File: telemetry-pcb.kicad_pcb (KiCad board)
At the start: 2 copper layers, 120 x 70 mm, 62 parts, among them CN1 12V, CN2 CAN, CN3 RS232, CN4 UART, CN5 THERMO1, CN6 THERMO2, CN7 CAN, IC1 MAX3232CPWR, IC2 MAX31855K, IC3 MAX31855K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

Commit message: added bottom silkscreen logo, date, and names
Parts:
- added G***: LOGO, telemetry-pcb:supermileage_logo, B.Cu at (104.9, 101.2)
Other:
- board text added: "Mar 4, 2022"
- board text added: "Silviu Toderita Leslie Cheng Valentino Jaber Colby Sparks Apoorv Garg"
- board text added: "Telemetry 2.0"

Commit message: deleted extraneous footprints
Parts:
- removed G***: LOGO, telemetry-pcb:supermileage_logo

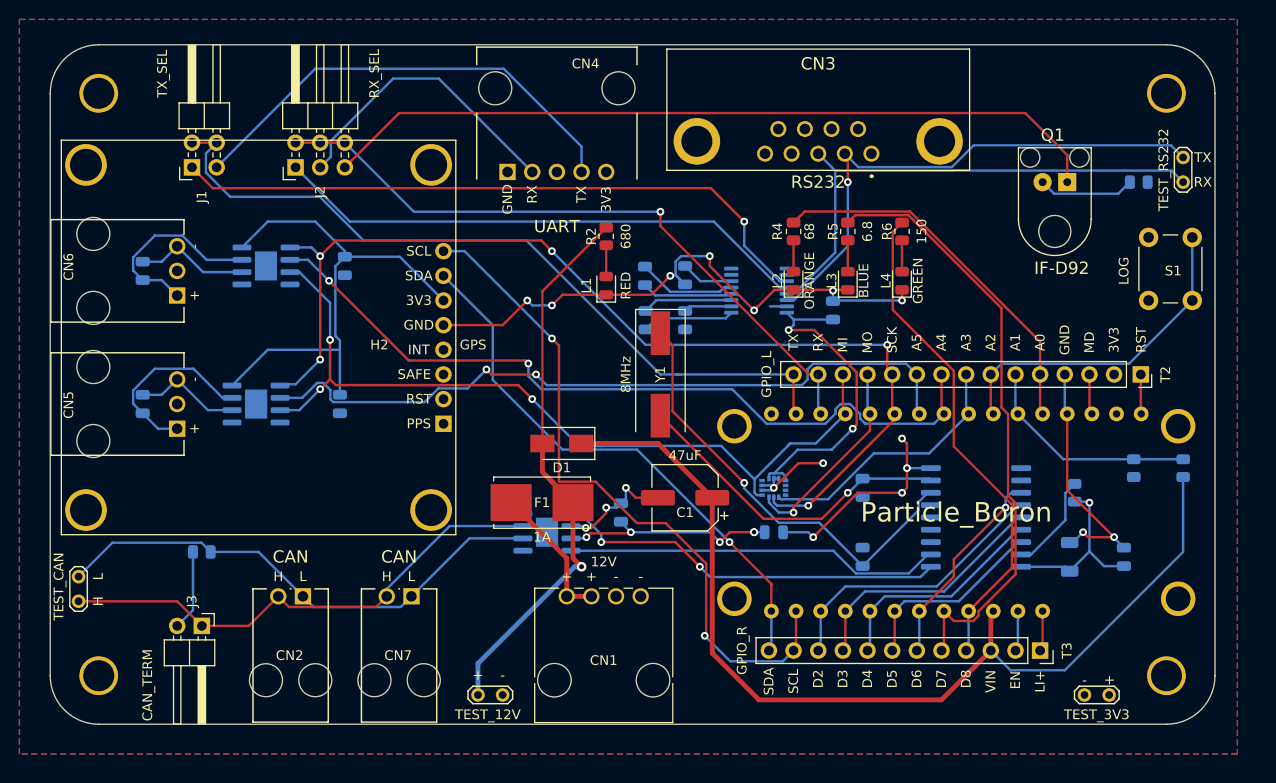
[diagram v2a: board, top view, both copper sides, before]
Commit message: Shrinks board and removes GPS. Replaces GPS with Qwiic connector for off-board GPS
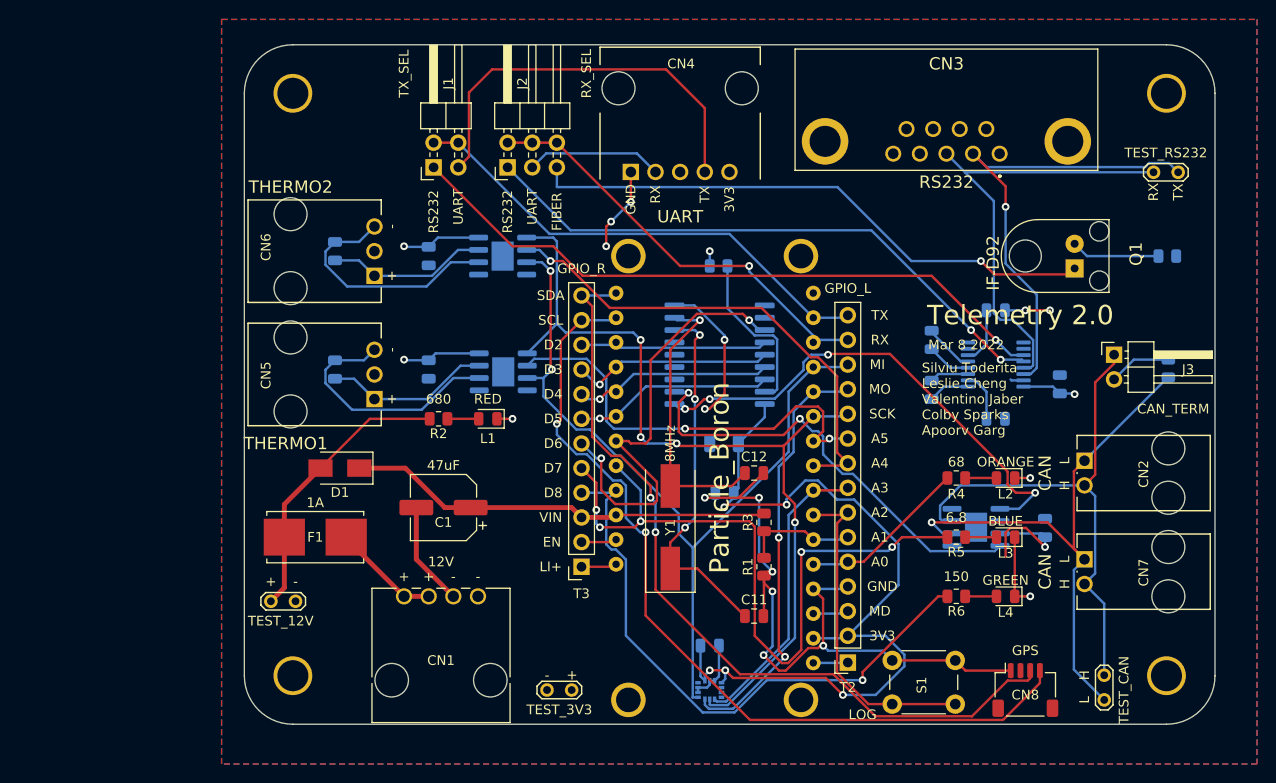
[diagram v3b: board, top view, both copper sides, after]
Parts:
- removed H2: GPS, telemetry-pcb:Sparkfun GPS
- added CN8: GPS, Connector_JST:JST_SH_SM04B-SRSS-TB_1x04-1MP_P1.00mm_Horizontal, F.Cu at (170.5, 121.5)
- added G***: LOGO, Footprints:sm-logo-small, B.Cu at (107.0, 102.7)
- C11, C12, R1, R3: moved to F.Cu
- moved T6 106.4 mm to (178.6, 122.5), turned to 90 degrees
- moved R9 101.3 mm to (185.2, 88.4), turned to 270 degrees
- moved J3 98.0 mm to (179.6, 86.9), turned to 0 degrees
- moved CN2 89.9 mm to (182.7, 99.1), turned to 90 degrees
- moved CN7 77.2 mm to (182.7, 109.3), turned to 90 degrees
- moved T4 55.4 mm to (123.7, 121.5)
- moved T3 48.0 mm to (124.7, 108.8), turned to 180 degrees
- moved S1 45.5 mm to (156.7, 118.4), turned to 0 degrees
- moved IC5 44.2 mm to (165.4, 104.7)
- moved C16 43.7 mm to (172.5, 104.8)
- moved R3 43.5 mm to (143.5, 104.2), turned to 90 degrees
- moved R8 43.5 mm to (138.9, 77.8), turned to 180 degrees
- moved T2 42.0 mm to (152.2, 118.4), turned to 180 degrees
- moved C13 41.7 mm to (139.5, 101.2), turned to 0 degrees
- moved R1 39.4 mm to (143.5, 108.8)
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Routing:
- net /VIN: track 102.2 -> 44.0 mm
- net /A4: track 81.9 -> 50.4 mm, vias 2 -> 1
- net /A5: track 75.8 -> 44.6 mm
- net /TX: track 80.0 -> 50.2 mm
- net Net-(D1-Pad2): track 57.6 -> 29.2 mm, vias 1 -> 0
- net /SDA: track 57.2 -> 84.1 mm, vias 1 -> 2
- net /D6: track 21.3 -> 46.7 mm, vias 1 -> 2
- net /RX: track 68.8 -> 44.4 mm
- net /MO: track 21.1 -> 43.9 mm, vias 1 -> 2
- net Net-(J2-Pad5): track 81.3 -> 59.4 mm, vias 0 -> 1
- net /A0: track 39.0 -> 17.5 mm
- net /SCL: track 71.0 -> 88.3 mm
- net /SCK: track 107.7 -> 91.0 mm, vias 5 -> 4
- net Net-(CN4-Pad2): track 30.6 -> 14.1 mm
- net Net-(C7-Pad1): track 11.2 -> 25.6 mm
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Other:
- board size 120 x 70 mm -> 100 x 70 mm
- board text added: "Mar 8 2022"
- board text removed: "Mar 4, 2022"

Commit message: changes CAN ports to 3 pin, Thermocouple ports to 2 pin
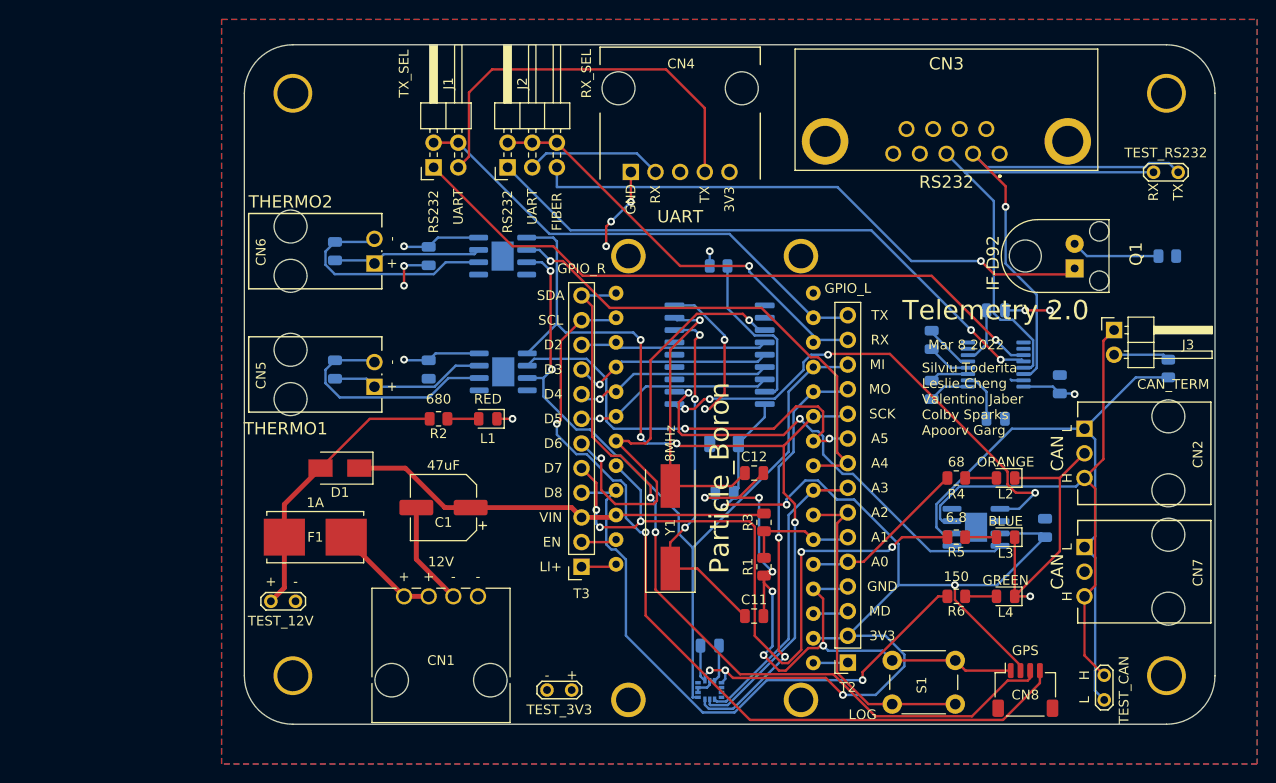
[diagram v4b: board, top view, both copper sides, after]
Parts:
- CN2, CN7: footprint telemetry-pcb:molex_sl_1x02_horizontal -> telemetry-pcb:molex-sl-1x03-horizontal
- CN5, CN6: footprint telemetry-pcb:molex-sl-1x03-horizontal -> telemetry-pcb:molex_sl_1x02_horizontal
- moved J3 2.54 mm to (179.6, 84.4)
- moved CN2 2.03 mm to (182.7, 97.1)
- moved G*** 1.61 mm to (106.5, 104.2), turned to 180 degrees
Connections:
- CN2 pad 2: Net-(CN2-Pad2) -> GND
- CN5 pad 2: Net-(CN5-Pad2) -> Net-(C7-Pad1)
- CN6 pad 2: Net-(CN6-Pad2) -> Net-(C8-Pad1)
- CN7 pad 2: Net-(CN2-Pad2) -> GND
- IC5 pad 7: Net-(CN2-Pad2) -> Net-(CN2-Pad3)
- J3 pad 1: Net-(CN2-Pad2) -> Net-(CN2-Pad3)
- T6 pad 2: Net-(CN2-Pad2) -> Net-(CN2-Pad3)
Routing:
- net Net-(CN2-Pad3): track 0.00 -> 57.3 mm
- net Net-(CN2-Pad2): track 54.4 -> 0.00 mm
- net GND: track 127.6 -> 152.9 mm, vias 16 -> 17
- net +3V3: track 123.1 -> 143.3 mm
- net Net-(CN2-Pad1): track 59.4 -> 63.3 mm, vias 1 -> 0
- net Net-(C8-Pad1): track 25.2 -> 23.6 mm
- net Net-(C7-Pad1): track 25.6 -> 24.2 mm
- net Net-(C7-Pad2): track 17.2 -> 16.1 mm
- net Net-(C8-Pad2): track 16.6 -> 15.5 mm
- net Net-(J3-Pad2): track 6.43 -> 5.80 mm

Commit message: minor changes to serial port - update rs232 connector and delete GND connection
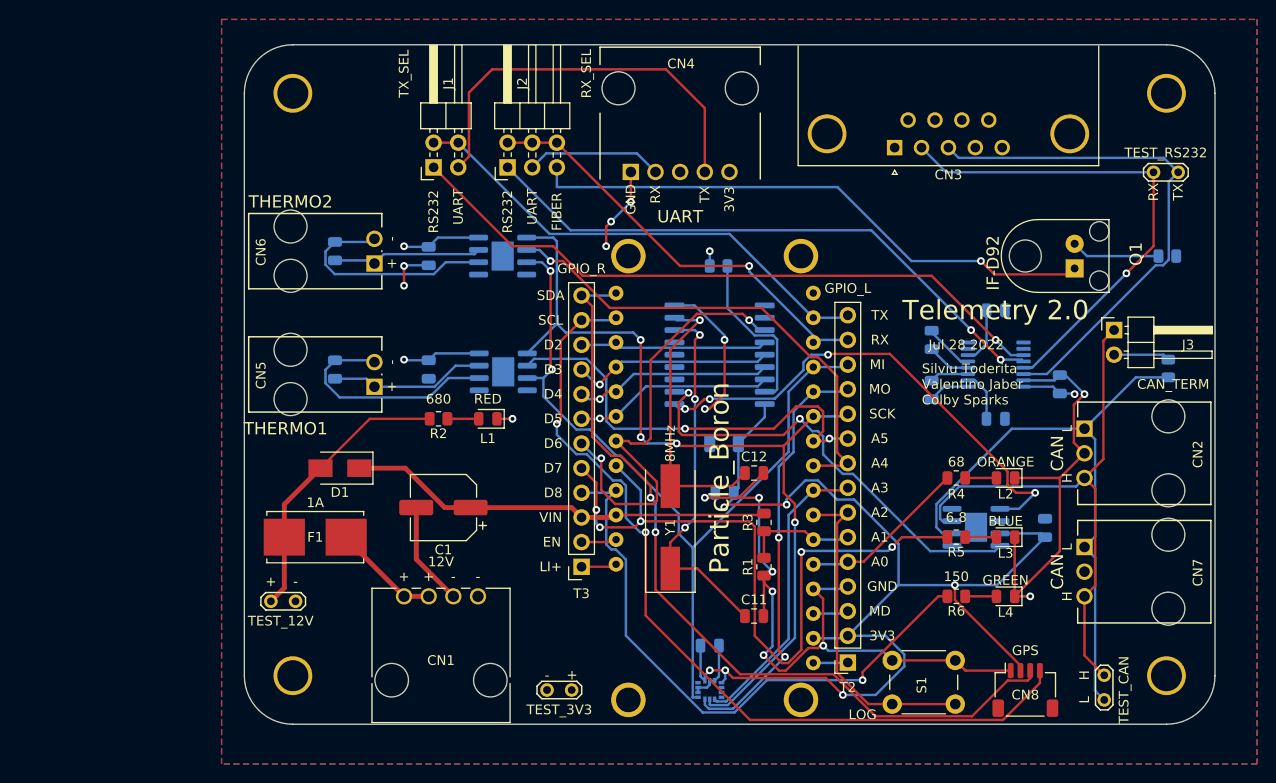
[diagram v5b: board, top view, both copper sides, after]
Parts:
- removed G***: LOGO, Footprints:sm-logo-small
- CN3: footprint telemetry-pcb:db-9 -> Connector_Dsub:DSUB-9_Female_Horizontal_P2.77x2.84mm_EdgePinOffset7.70mm_Housed_MountingHolesOffset9.12mm
- moved CN3 6.41 mm to (157.0, 65.6)
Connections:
- CN3 pad 5: GND -> Net-(CN3-Pad5)
- IC1 pad 13: Net-(CN3-Pad3) -> Net-(CN3-Pad2)
- IC1 pad 14: Net-(CN3-Pad2) -> Net-(CN3-Pad3)
- T5 pad 1: Net-(CN3-Pad2) -> Net-(CN3-Pad3)
- T5 pad 2: Net-(CN3-Pad3) -> Net-(CN3-Pad2)
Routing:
- net GND: track 152.9 -> 161.2 mm, vias 17 -> 16
- net Net-(CN3-Pad3): track 46.8 -> 54.7 mm
- net Net-(CN3-Pad2): track 48.7 -> 51.8 mm
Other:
- board text added: "(down)"
- board text added: "Jul 28 2022"
- board text added: "Silviu Toderita Valentino Jaber Colby Sparks"
- board text added: "x"
- board text added: "y"
- board text added: "z"
- board text removed: "Mar 8 2022"
- board text removed: "Silviu Toderita Leslie Cheng Valentino Jaber Colby Sparks Apoorv Garg"

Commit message: fixes optical receiver wiring and changes GPS connector to JST GH
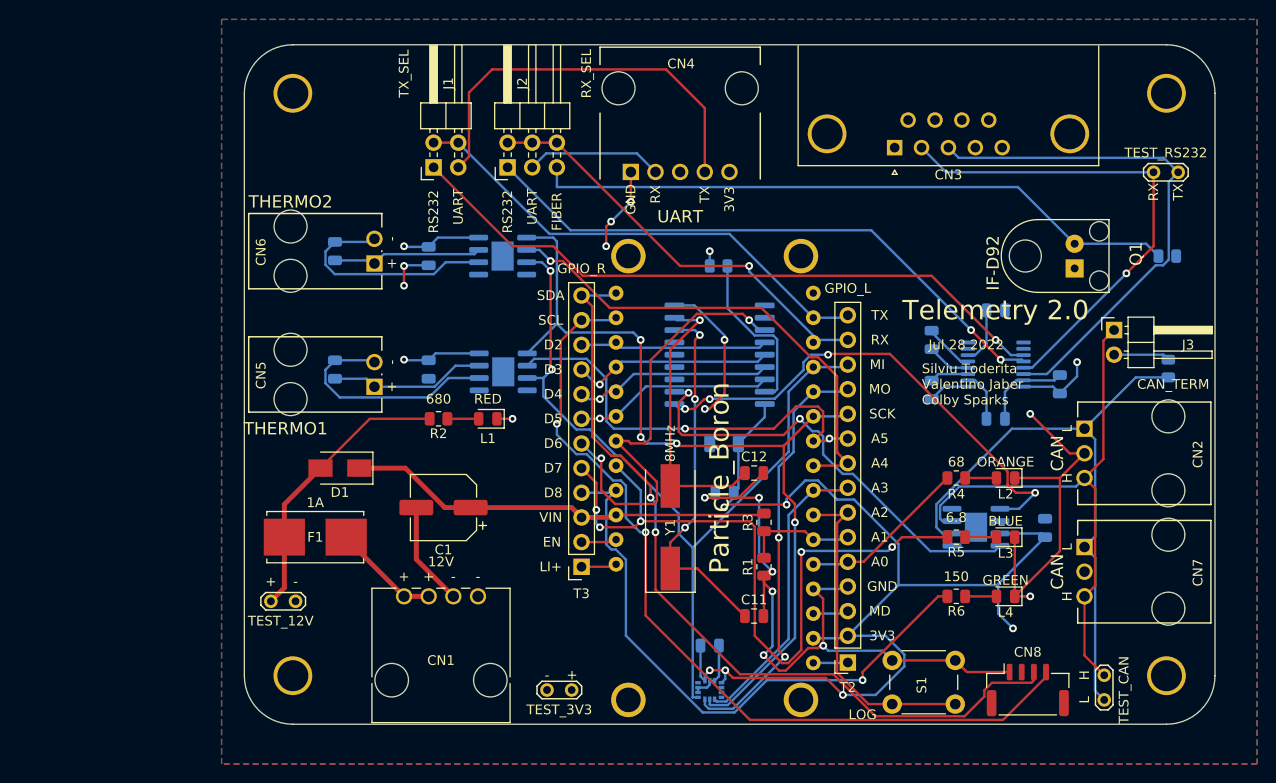
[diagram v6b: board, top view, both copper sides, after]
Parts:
- CN8: footprint Connector_JST:JST_SH_SM04B-SRSS-TB_1x04-1MP_P1.00mm_Horizontal -> Connector_JST:JST_GH_SM04B-GHS-TB_1x04-1MP_P1.25mm_Horizontal
- moved CN8 0.25 mm to (170.7, 121.5)
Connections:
- Q1 pad 1: Net-(J2-Pad5) -> +3V3
- Q1 pad 2: Net-(Q1-Pad2) -> Net-(J2-Pad5)
- R7 pad 1: Net-(Q1-Pad2) -> Net-(J2-Pad5)
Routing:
- net Net-(Q1-Pad2): track 9.16 -> 0.00 mm
- net Net-(J2-Pad5): track 59.4 -> 67.0 mm, vias 1 -> 0
- net GND: track 161.2 -> 163.8 mm
- net +3V3: track 143.3 -> 140.7 mm
- net /SDA: track 84.1 -> 84.8 mm

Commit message: some more small changes from design review
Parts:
- CN1: footprint telemetry-pcb:molex_sl_1x04_horizontal -> telemetry-pcb:molex_sl_1x02_horizontal
- CN4: footprint telemetry-pcb:Molex-70551-0004-0 -> telemetry-pcb:molex_sl_1x04_horizontal
- CN5, CN6: footprint telemetry-pcb:molex_sl_1x02_horizontal -> telemetry-pcb:ScrewTermPlug1x02
- moved C1 13.3 mm to (116.9, 114.4)
- moved D1 13.0 mm to (112.0, 103.2)
- moved CN1 10.8 mm to (105.2, 117.9), turned to 0 degrees
- moved CN4 6.60 mm to (132.4, 68.1), turned to 0 degrees
- moved C8 6.45 mm to (94.0, 72.6), turned to 90 degrees
- moved C7 6.02 mm to (94.0, 91.2), turned to 90 degrees
- moved CN6 3.39 mm to (98.1, 73.0)
- moved CN5 2.41 mm to (98.1, 91.2)
- moved F1 0.80 mm to (97.1, 105.0), turned to 0 degrees
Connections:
- CN1 pad 2: GND -> Net-(CN1-Pad2)
- CN4 pad 4: Net-(CN4-Pad4) -> +3V3
- CN4 pad 5: +3V3 -> (no net)
- F1 pad 1: Net-(CN1-Pad3) -> Net-(CN1-Pad2)
- J1 pad 3: Net-(CN4-Pad4) -> Net-(CN4-Pad3)
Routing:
- net Net-(CN4-Pad4): track 41.7 -> 0.00 mm
- net Net-(CN4-Pad3): track 0.00 -> 29.9 mm
- net Net-(CN1-Pad2): track 0.00 -> 12.9 mm
- net +3V3: track 140.7 -> 153.4 mm, vias 10 -> 11
- net Net-(D1-Pad2): track 29.2 -> 41.7 mm
- net Net-(CN1-Pad3): track 11.1 -> 0.00 mm
- net GND: track 163.8 -> 172.5 mm, vias 16 -> 14
- net Net-(C8-Pad2): track 15.5 -> 22.7 mm
- net Net-(C7-Pad2): track 16.1 -> 21.1 mm
- net Net-(CN4-Pad2): track 14.1 -> 17.3 mm
- net Net-(C7-Pad1): track 24.2 -> 22.0 mm
- net /VIN: track 44.0 -> 42.6 mm
- net Net-(C8-Pad1): track 23.6 -> 22.3 mm
- net Net-(C4-Pad1): track 5.84 -> 6.49 mm

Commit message: 2-0 complete
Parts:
- added G***: LOGO, telemetry-pcb:sm-logo-small, F.Cu at (161.1, 93.5)
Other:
- board text added: "Aug 9 2022"
- board text removed: "Jul 28 2022"
